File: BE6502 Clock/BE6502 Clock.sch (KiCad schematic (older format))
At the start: 29 parts, among them J1 CLOCK_SEL, M1 Mounting, M2 Mounting, M3 Mounting, M4 Mounting, SW1 MANUAL, SW2 CLK_SEL, U1 LM555, U2 LM555, U3 LM555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

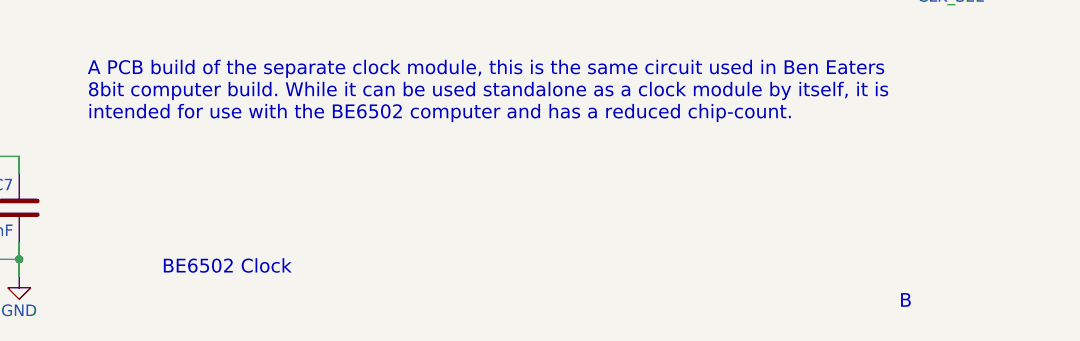
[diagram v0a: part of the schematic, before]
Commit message: Update errata and bump module revision number
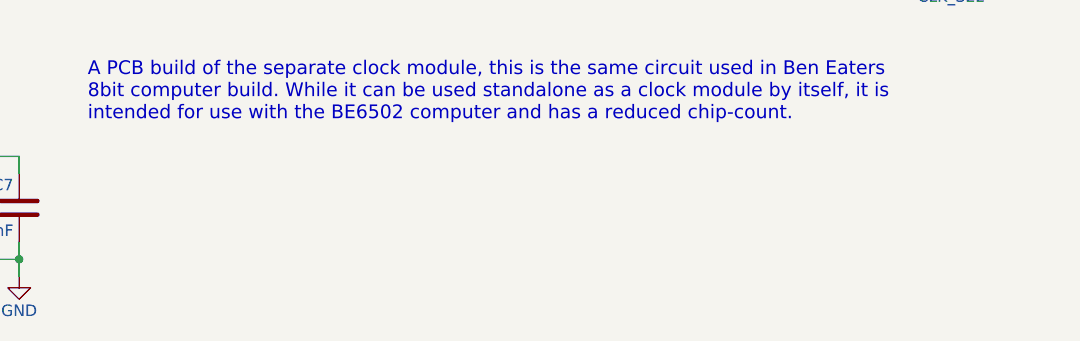
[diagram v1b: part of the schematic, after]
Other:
- note removed: "B"
- note removed: "BE6502 Clock"
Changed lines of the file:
@@
 encoding utf-8
 Sheet 1 1
-Title ""
+Title "BE6502 Clock"
 Date ""
-Rev ""
+Rev "C"
 Comp ""
 Comment1 ""
@@
 	1    0    0    -1
 $EndComp
-Text Notes 12175 10925 0    60   ~ 0
-BE6502 Clock
-Text Notes 15400 11075 0    60   ~ 0
-B
 Text GLabel 3925 2725 2    60   Input ~ 0
 CLOCK_OUT
